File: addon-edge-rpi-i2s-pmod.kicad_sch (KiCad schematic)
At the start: 35 parts, among them J1 PMOD1, J10 Conn_01x02, J12 Conn_01x02, J13 Conn_01x01, J2 PMOD2, J3 PMOD3, J4 PMOD4, J5 Conn_01x06, J6 Conn_01x06, J7 Conn_01x03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

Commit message: v1.00 minor changes after testing manufactured v0.7
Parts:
- J3: renamed from J4; value PMOD4 -> PMOD3
- J4: renamed from J3; value PMOD3 -> PMOD4
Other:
- note added: "PMOD 3"
- note added: "PMOD 4 (SPI+UART)"
- note removed: "PMOD 3 (SPI+UART)"
- note removed: "PMOD 4 (SRAM)"
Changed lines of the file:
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@@
     (effects (font (size 2.54 2.54)) (justify left bottom))
   )
-  (text "PMOD 4 (SRAM)" (at 80.01 158.75 0)
+  (text "PMOD 3" (at 88.265 158.115 0)
     (effects (font (size 2.54 2.54)) (justify left bottom))
   )
@@
     (effects (font (size 1.27 1.27)) (justify left bottom))
   )
-  (text "PMOD 3 (SPI+UART)" (at 79.375 117.475 0)
+  (text "PMOD 4 (SPI+UART)" (at 74.295 118.11 0)
     (effects (font (size 2.54 2.54)) (justify left bottom))
   )
@@
   (symbol (lib_id "Connector_Generic:Conn_02x06_Top_Bottom") (at 93.345 131.445 0) (unit 1)
     (in_bom yes) (on_board yes)
-    (property "Reference" "J3" (id 0) (at 94.615 120.8532 0))
-    (property "Value" "PMOD3" (id 1) (at 94.615 123.1646 0))
+    (property "Reference" "J4" (id 0) (at 94.615 120.8532 0))
+    (property "Value" "PMOD4" (id 1) (at 94.615 123.1646 0))
     (property "Footprint" "gomaDOSzero:PMOD_Female_Horizontal_2" (id 2) (at 93.345 131.445 0)
       (effects (font (size 1.27 1.27)) hide)
@@
   (symbol (lib_id "Connector_Generic:Conn_02x06_Top_Bottom") (at 93.345 171.45 0) (unit 1)
     (in_bom yes) (on_board yes)
-    (property "Reference" "J4" (id 0) (at 94.615 160.8582 0))
-    (property "Value" "PMOD4" (id 1) (at 94.615 163.1696 0))
+    (property "Reference" "J3" (id 0) (at 94.615 160.8582 0))
+    (property "Value" "PMOD3" (id 1) (at 94.615 163.1696 0))
     (property "Footprint" "gomaDOSzero:PMOD_Female_Horizontal_2" (id 2) (at 93.345 171.45 0)
       (effects (font (size 1.27 1.27)) hide)
@@
       (reference "J2") (unit 1) (value "PMOD2") (footprint "gomaDOSzero:Pmod_2x06_P2.54mm_Vertical_2")
     )
+    (path "/974dc5f0-3500-4950-b40e-1dcd627496a2"
+      (reference "J3") (unit 1) (value "PMOD3") (footprint "gomaDOSzero:PMOD_Female_Horizontal_2")
+    )
     (path "/3e4369ed-61b9-4b9e-92f5-8943e3df62d1"
-      (reference "J3") (unit 1) (value "PMOD3") (footprint "gomaDOSzero:PMOD_Female_Horizontal_2")
-    )
-    (path "/974dc5f0-3500-4950-b40e-1dcd627496a2"
       (reference "J4") (unit 1) (value "PMOD4") (footprint "gomaDOSzero:PMOD_Female_Horizontal_2")
     )

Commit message: changed repository name
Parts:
- added JP31, JP32: (no value), symbol Connector_Generic:Conn_01x02
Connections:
- net A1_MOSI: now also JP31.1 (Pin_1)
- net A2_CE1: now also JP32.1 (Pin_1)
- net SCL_RPI: now also JP32.2 (Pin_2)
- net SDA_RPI: now also JP31.2 (Pin_2)
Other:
- note added: "JUMPER 5"
- note added: "JUMPERS 3 I2C / SPI"
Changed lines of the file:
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@@
+    (stroke (width 0) (type default) (color 0 0 0 0))
+  )
+  (wire (pts (xy 226.06 250.825) (xy 248.92 250.825))
     (stroke (width 0) (type default) (color 0 0 0 0))
   )
@@
     (stroke (width 0) (type default) (color 0 0 0 0))
   )
+  (wire (pts (xy 226.06 264.795) (xy 248.92 264.795))
+    (stroke (width 0) (type default) (color 0 0 0 0))
+  )
   (wire (pts (xy 52.705 153.67) (xy 58.42 153.67))
     (stroke (width 0) (type default) (color 0 0 0 0))
@@
     (stroke (width 0) (type default) (color 0 0 0 0))
   )
+  (wire (pts (xy 251.46 250.825) (xy 273.05 250.825))
+    (stroke (width 0) (type default) (color 0 0 0 0))
+  )
   (wire (pts (xy 66.675 126.365) (xy 88.265 126.365))
     (stroke (width 0) (type default) (color 0 0 0 0))
@@
     (stroke (width 0) (type default) (color 0 0 0 0))
   )
+  (wire (pts (xy 251.46 264.795) (xy 273.05 264.795))
+    (stroke (width 0) (type default) (color 0 0 0 0))
+  )
   (wire (pts (xy 290.195 193.04) (xy 290.195 189.23))
     (stroke (width 0) (type default) (color 0 0 0 0))
@@
     (stroke (width 0) (type default) (color 0 0 0 0))
   )
+  (polyline (pts (xy 213.995 278.765) (xy 283.845 278.765))
+    (stroke (width 0) (type default) (color 0 0 0 0))
+  )
   (wire (pts (xy 114.935 93.98) (xy 137.795 93.98))
     (stroke (width 0) (type default) (color 0 0 0 0))
@@
   )
   (wire (pts (xy 297.815 161.29) (xy 297.815 165.1))
+    (stroke (width 0) (type default) (color 0 0 0 0))
+  )
+  (polyline (pts (xy 283.845 233.68) (xy 283.845 278.765))
     (stroke (width 0) (type default) (color 0 0 0 0))
   )
@@
     (effects (font (size 2.54 2.54)) (justify left bottom))
   )
+  (text "JUMPERS 3 I2C / SPI" (at 229.235 241.935 0)
+    (effects (font (size 2.54 2.54)) (justify left bottom))
+  )
   (text "UART" (at 178.435 220.345 0)
     (effects (font (size 2.54 2.54)) (justify left bottom))
@@
     (effects (font (size 1.27 1.27)) (justify left bottom))
   )
+  (text "JUMPER 5" (at 132.715 155.575 0)
+    (effects (font (size 2 2)) (justify left bottom))
+  )
   (text "ROTATIVE ENCODER" (at 56.515 248.285 0)
     (effects (font (size 1.27 1.27)) (justify left bottom))
@@
     (effects (font (size 1.27 1.27)) (justify left bottom))
   )
+  (label "A2_CE1" (at 226.06 264.795 0)
+    (effects (font (size 1.2446 1.2446)) (justify left bottom))
+  )
   (label "A1_MOSI" (at 167.005 125.095 0)
     (effects (font (size 1.2446 1.2446)) (justify left bottom))
@@
     (effects (font (size 1.27 1.27)) (justify left bottom))
   )
+  (label "SCL_RPI" (at 265.43 264.795 0)
+    (effects (font (size 1.2446 1.2446)) (justify left bottom))
+  )
   (label "SCL_RPI" (at 249.555 43.18 0)
     (effects (font (size 1.2446 1.2446)) (justify left bottom))
@@
     (effects (font (size 1.27 1.27)) (justify left bottom))
   )
+  (label "SDA_RPI" (at 265.43 250.825 0)
+    (effects (font (size 1.2446 1.2446)) (justify left bottom))
+  )
   (label "B13_SCLK_DABD" (at 167.005 81.915 0)
     (effects (font (size 1.2446 1.2446)) (justify left bottom))
@@
   (label "DISPLAY_PS1" (at 114.3 223.52 0)
     (effects (font (size 1.27 1.27)) (justify left bottom))
+  )
+  (label "A1_MOSI" (at 226.06 250.825 0)
+    (effects (font (size 1.2446 1.2446)) (justify left bottom))
   )
   (label "B19_PMOD2_D0" (at 101.6 76.2 0)
@@
     (pin "1")
   )
+  (symbol (lib_id "Connector_Generic:Conn_01x02") (at 248.92 269.875 90) (mirror x) (unit 1)
+    (in_bom yes) (on_board yes)
+    (property "Reference" "JP32" (id 0) (at 246.38 269.875 90)
+      (effects (font (size 1.27 1.27)) (justify left))
+    )
+    (property "Value" "" (id 1) (at 255.27 273.05 90)
+      (effects (font (size 1.27 1.27)) (justify left))
+    )
+    (property "Footprint" "" (id 2) (at 248.92 269.875 0)
+      (effects (font (size 1.27 1.27)) hide)
+    )
+    (property "Datasheet" "~" (id 3) (at 248.92 269.875 0)
+      (effects (font (size 1.27 1.27)) hide)
+    )
+    (pin "1")
+    (pin "2")
+  )
+  (symbol (lib_id "Connector_Generic:Conn_01x02") (at 248.92 255.905 90) (mirror x) (unit 1)
+    (in_bom yes) (on_board yes)
+    (property "Reference" "JP31" (id 0) (at 246.38 255.905 90)
+      (effects (font (size 1.27 1.27)) (justify left))
+    )
+    (property "Value" "" (id 1) (at 255.27 259.08 90)
+      (effects (font (size 1.27 1.27)) (justify left))
+    )
+    (property "Footprint" "" (id 2) (at 248.92 255.905 0)
+      (effects (font (size 1.27 1.27)) hide)
+    )
+    (property "Datasheet" "~" (id 3) (at 248.92 255.905 0)
+      (effects (font (size 1.27 1.27)) hide)
+    )
+    (pin "1")
+    (pin "2")
+  )
   (symbol (lib_id "power:GND") (at 353.695 132.715 0) (unit 1)
     (in_bom yes) (on_board yes)
@@
       (reference "JP23") (unit 1) (value "Conn_01x03") (footprint "Connector_PinHeader_2.54mm:PinHeader_1x03_P2.54mm_Horizontal")
     )
+    (path "/db8ba921-fbc6-4bbd-be19-bba7888e3e84"
+      (reference "JP31") (unit 1) (value "Conn_01x02") (footprint "Connector_PinHeader_2.54mm:PinHeader_1x02_P2.54mm_Vertical")
+    )
+    (path "/d5d56b0a-a130-4cfd-98ef-27748af309b1"
+      (reference "JP32") (unit 1) (value "Conn_01x02") (footprint "Connector_PinHeader_2.54mm:PinHeader_1x02_P2.54mm_Vertical")
+    )
     (path "/91d4baa6-de13-4b15-a05c-349d000f9daa"

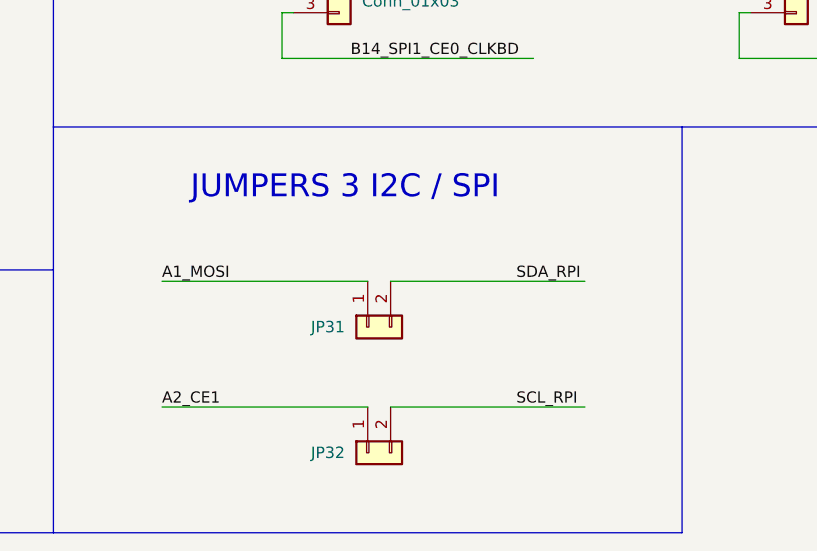
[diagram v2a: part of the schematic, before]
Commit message: v1.10 added i2c jumpers to control mt32-pi from fpga
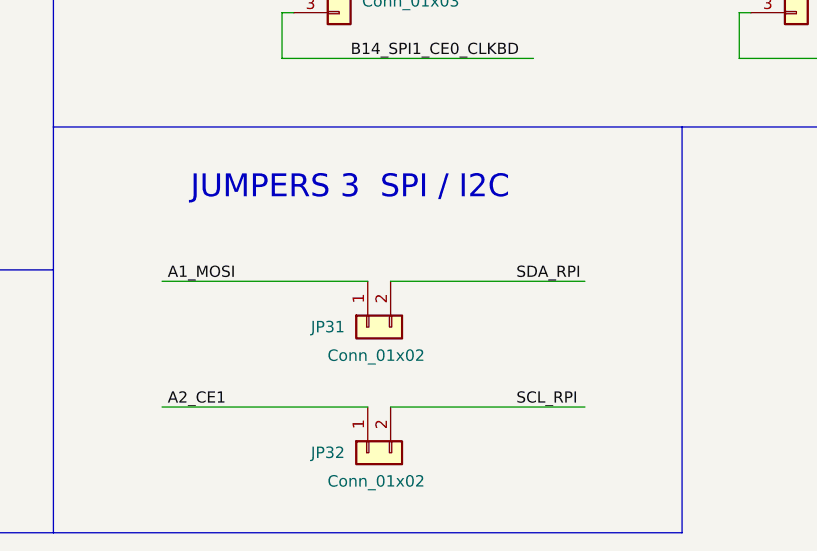
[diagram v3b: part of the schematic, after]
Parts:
- JP31, JP32: value (none) -> Conn_01x02; footprint (none) -> Connector_PinHeader_2.54mm:PinHeader_1x02_P2.54mm_Vertical
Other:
- note added: "JUMPERS 3 SPI / I2C"
- note removed: "JUMPERS 3 I2C / SPI"
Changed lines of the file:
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@@
     (effects (font (size 2.54 2.54)) (justify left bottom))
   )
-  (text "JUMPERS 3 I2C / SPI" (at 229.235 241.935 0)
+  (text "JUMPERS 3  SPI / I2C" (at 229.235 241.935 0)
     (effects (font (size 2.54 2.54)) (justify left bottom))
   )
@@
     (effects (font (size 1.27 1.27)) (justify left bottom))
   )
-  (label "A2_CE1" (at 226.06 264.795 0)
+  (label "A2_CE1" (at 226.695 264.795 0)
     (effects (font (size 1.2446 1.2446)) (justify left bottom))
   )
@@
     (effects (font (size 1.27 1.27)) (justify left bottom))
   )
-  (label "A1_MOSI" (at 226.06 250.825 0)
+  (label "A1_MOSI" (at 226.695 250.825 0)
     (effects (font (size 1.2446 1.2446)) (justify left bottom))
   )
@@
       (effects (font (size 1.27 1.27)) (justify left))
     )
-    (property "Value" "" (id 1) (at 255.27 273.05 90)
-      (effects (font (size 1.27 1.27)) (justify left))
-    )
-    (property "Footprint" "" (id 2) (at 248.92 269.875 0)
+    (property "Value" "Conn_01x02" (id 1) (at 255.27 273.05 90)
+      (effects (font (size 1.27 1.27)) (justify left))
+    )
+    (property "Footprint" "Connector_PinHeader_2.54mm:PinHeader_1x02_P2.54mm_Vertical" (id 2) (at 248.92 269.875 0)
       (effects (font (size 1.27 1.27)) hide)
     )
@@
       (effects (font (size 1.27 1.27)) (justify left))
     )
-    (property "Value" "" (id 1) (at 255.27 259.08 90)
-      (effects (font (size 1.27 1.27)) (justify left))
-    )
-    (property "Footprint" "" (id 2) (at 248.92 255.905 0)
-      (effects (font (size 1.27 1.27)) hide)
-    )
+    (property "Value" "Conn_01x02" (id 1) (at 255.27 259.08 90)
+      (effects (font (size 1.27 1.27)) (justify left))
+    )
+    (property "Footprint" "Connector_PinHeader_2.54mm:PinHeader_1x02_P2.54mm_Vertical" (id 2) (at 248.92 255.905 0)
+      (effects (font (size 1.27 1.27)) hide)
+    )
